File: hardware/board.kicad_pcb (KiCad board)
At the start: 2 copper layers, 79 x 58 mm, 37 parts, among them J1 Screw_Terminal_01x02, J2 Conn_JTAG, Q1 2SC1815, U1 FT2232D, U2 SN74AVC4T245PW, U3 SN74AVC4T245PW, U4 SN74AVC4T245PW

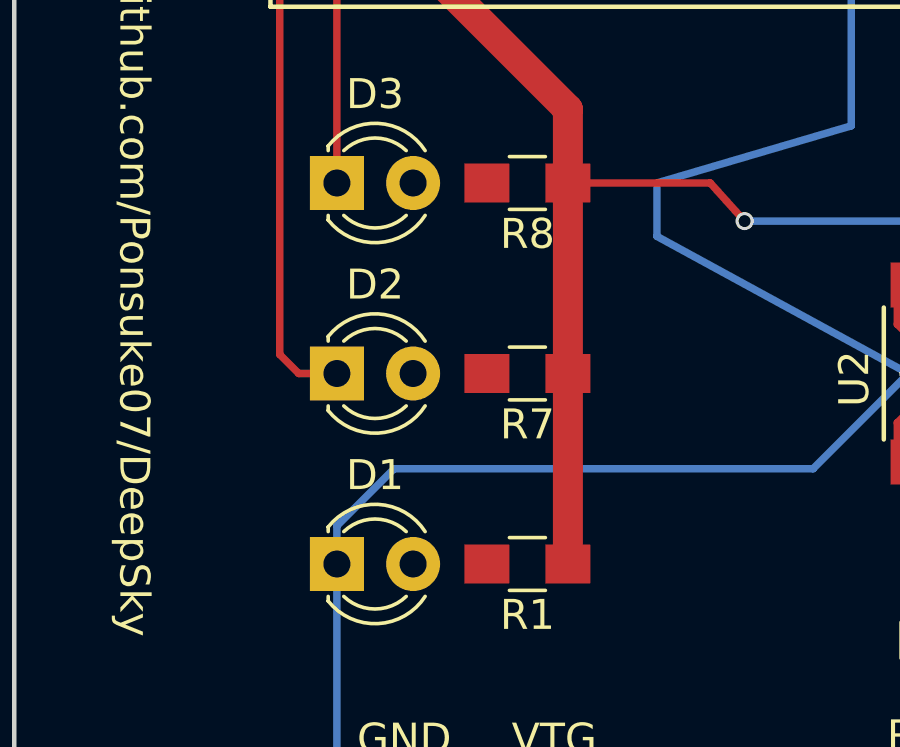
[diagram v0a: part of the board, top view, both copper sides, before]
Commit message: hardware: Fix connection of LED
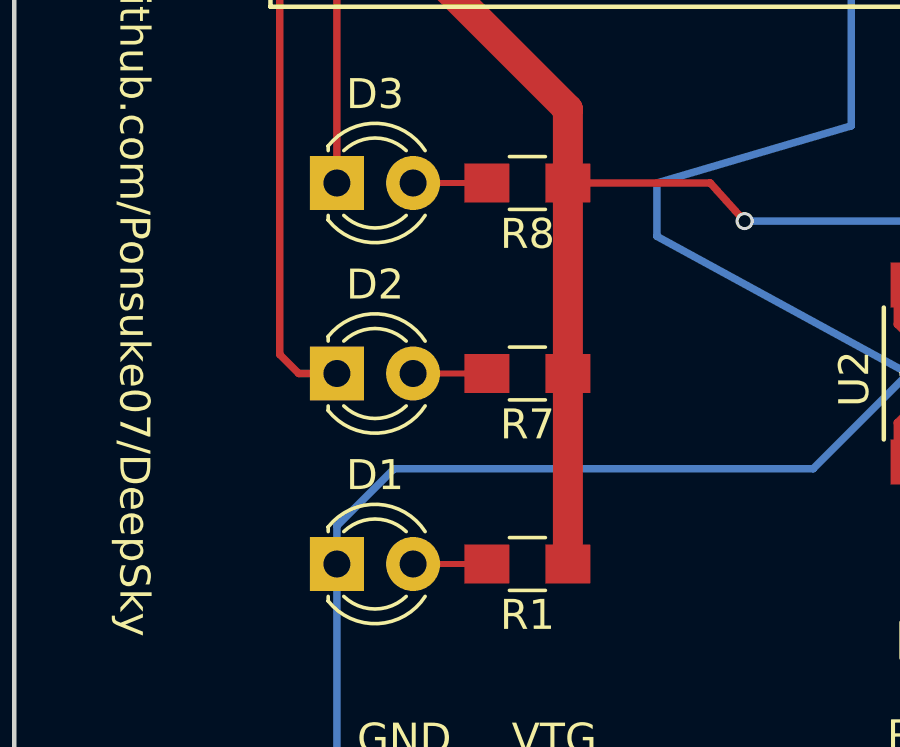
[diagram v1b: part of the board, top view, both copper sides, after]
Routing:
- net Net-(D3-Pad2): track 0.00 -> 2.46 mm
- net Net-(D2-Pad2): track 0.00 -> 2.46 mm
- net Net-(D1-Pad2): track 0.00 -> 2.46 mm
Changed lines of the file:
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@@
   (general
     (links 108)
-    (no_connects 3)
+    (no_connects 0)
     (area 98.924999 72.924999 189.85 137.700001)
     (thickness 1.6)
     (drawings 11)
-    (tracks 392)
+    (tracks 395)
     (zones 0)
     (modules 37)
@@
   )
   (setup
-    (last_trace_width 0.25)
+    (last_trace_width 0.2)
     (user_trace_width 0.2)
     (user_trace_width 0.5)
@@
   (segment (start 134.52 112.27) (end 135.155 111.635) (width 0.2) (layer F.Cu) (net 3))
   (segment (start 135.155 111.635) (end 135.155 110.98) (width 0.2) (layer F.Cu) (net 3))
+  (segment (start 112.295 114.175) (end 114.755 114.175) (width 0.2) (layer F.Cu) (net 4) (status C00000))
   (segment (start 130.71 88.775) (end 137.695 88.775) (width 0.25) (layer B.Cu) (net 5))
   (segment (start 150.395 88.775) (end 137.695 88.775) (width 0.25) (layer F.Cu) (net 5))
@@
   (segment (start 168.81 100.84) (end 167.54 102.11) (width 1) (layer F.Cu) (net 5))
   (segment (start 167.54 102.11) (end 166.27 102.11) (width 1) (layer F.Cu) (net 5))
+  (segment (start 112.295 107.825) (end 114.755 107.825) (width 0.2) (layer F.Cu) (net 6) (status C00000))
   (segment (start 130.71 90.045) (end 137.695 90.045) (width 0.25) (layer B.Cu) (net 7))
   (segment (start 149.125 98.935) (end 142.775 98.935) (width 0.25) (layer B.Cu) (net 7))
@@
   (segment (start 148.49 90.045) (end 149.76 91.315) (width 0.25) (layer F.Cu) (net 7))
   (segment (start 148.49 90.045) (end 148.49 90.045) (width 0.25) (layer F.Cu) (net 7))
+  (segment (start 112.295 101.475) (end 114.755 101.475) (width 0.2) (layer F.Cu) (net 8) (status C00000))
   (segment (start 132.615 119.89) (end 152.935 119.89) (width 0.25) (layer B.Cu) (net 9))
   (segment (start 131.98 118.065) (end 131.98 119.255) (width 0.25) (layer F.Cu) (net 9))

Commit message: hardware: Minor update v1.0.1
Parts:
- renumbered D1 to PWD, D3 to SRST, D2 to VTG
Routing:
- net VCC: track 163.9 -> 166.0 mm, vias 6 -> 4
- net /TDI: track 19.8 -> 18.3 mm
- net /nSRST_IN: track 69.9 -> 68.6 mm, vias 4 -> 6
- net /TDO: track 27.4 -> 26.5 mm
- net /nSRST: track 20.9 -> 21.6 mm, vias 0 -> 1
- net /RTCK: track 14.1 -> 13.4 mm
- net /nTRST: track 22.0 -> 21.7 mm, vias 0 -> 1
- net /nOE_SRST: track 29.2 -> 29.0 mm, vias 4 -> 0
- net /nTARGET_VCC: track 95.6 -> 95.7 mm, vias 2 -> 4
- net /TCK: track 22.5 -> 22.6 mm, vias 2 -> 1
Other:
- outline, holes or cut-outs redrawn
